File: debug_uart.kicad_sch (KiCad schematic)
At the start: 1 part, among them U1 NX1H35 PBGA625

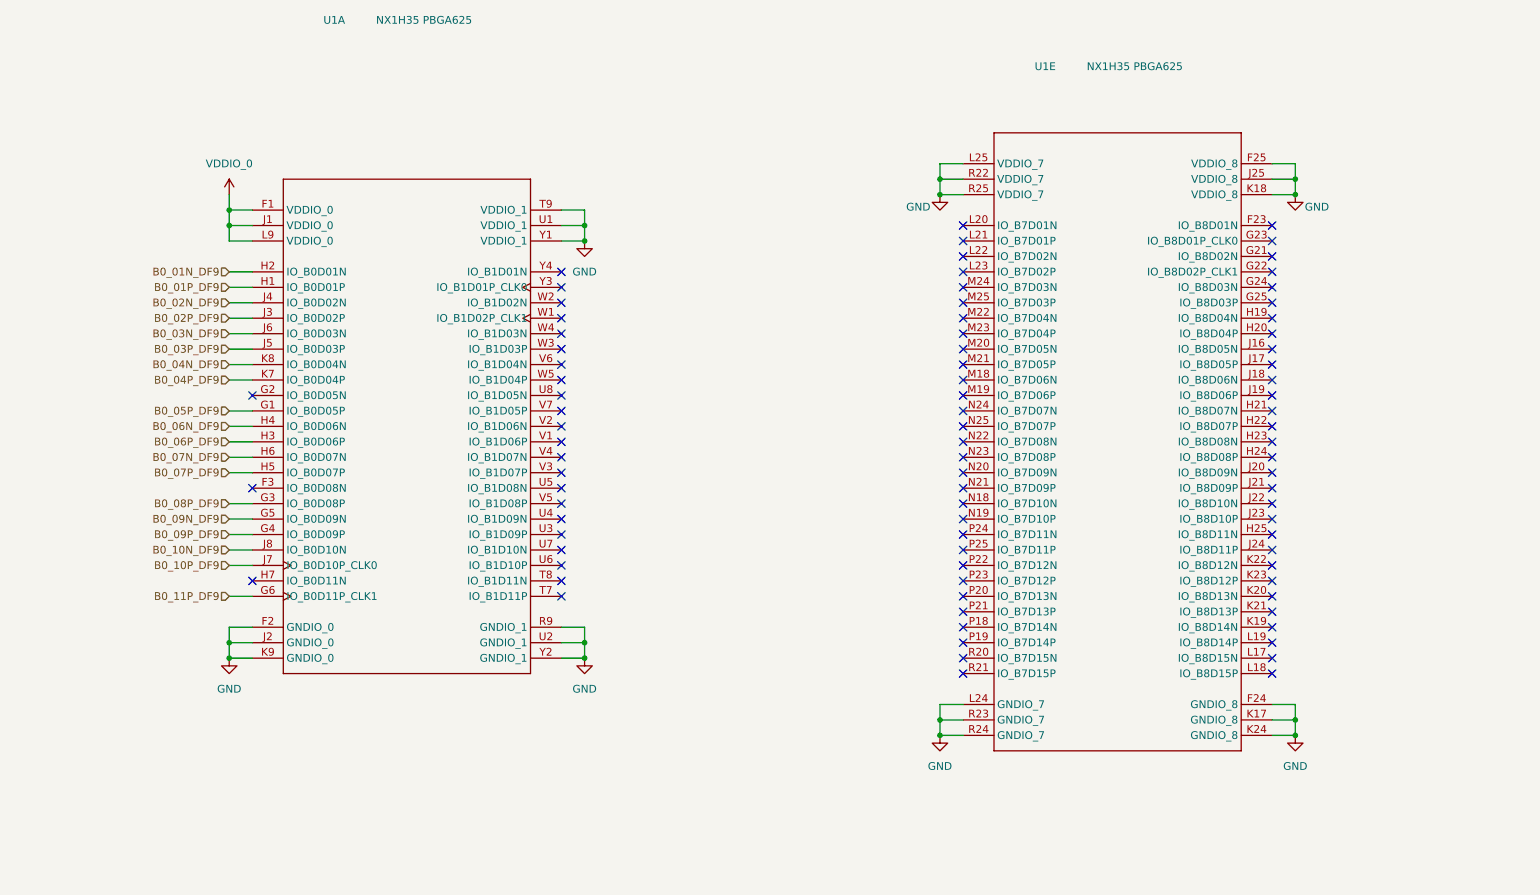
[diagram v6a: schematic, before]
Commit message: pre order adjustments. Board symmetry
adjusted little things brought up by DFM checker of JLCPCB. Board's edges fully symmetrical on y axis. 2mm shift on x axis of the DF9s maintained
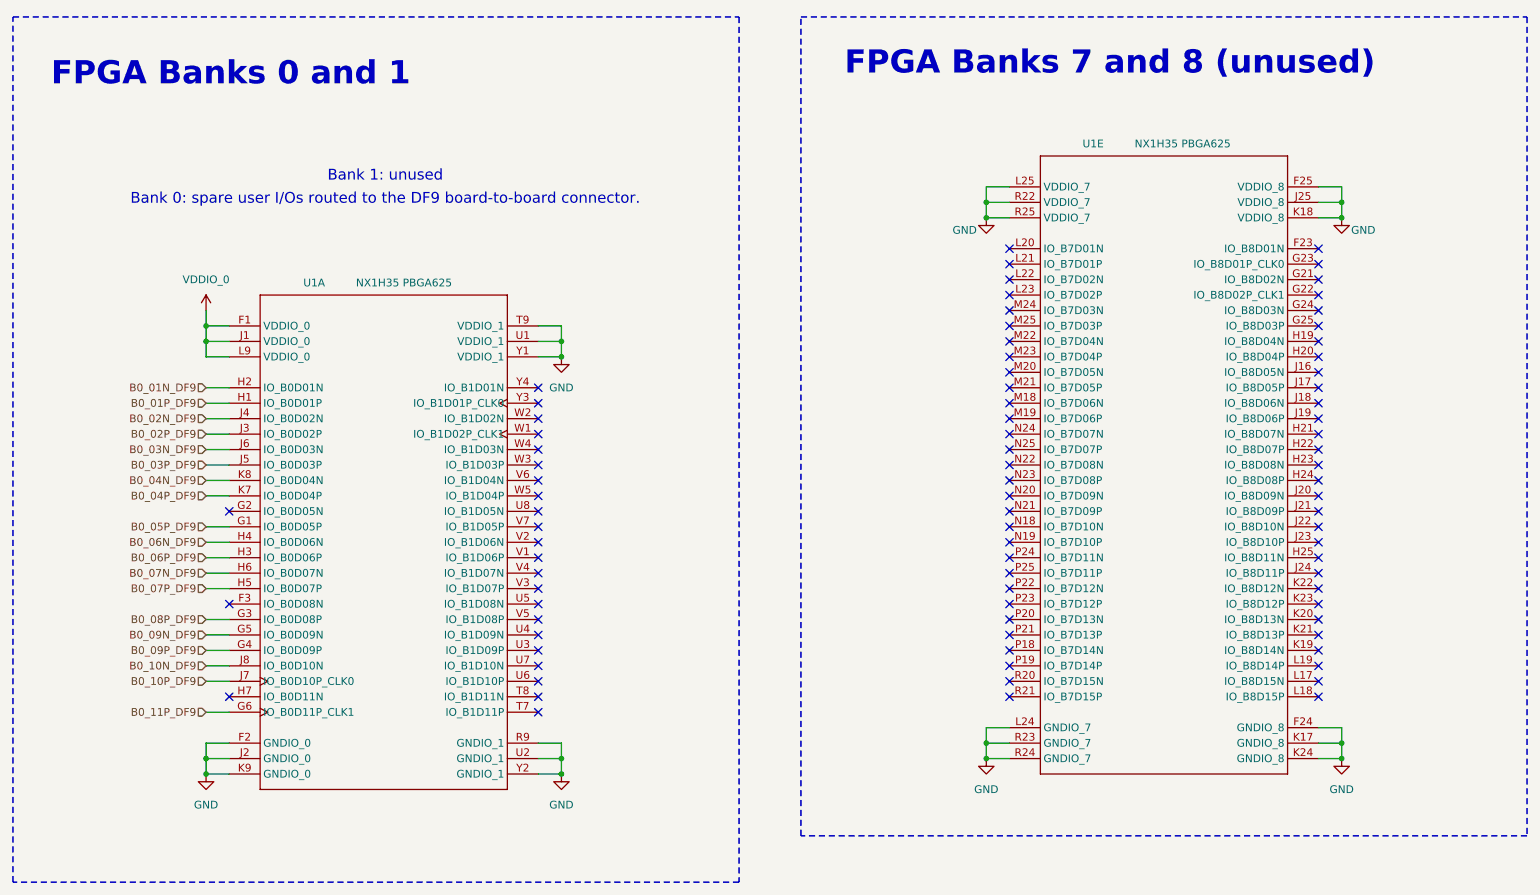
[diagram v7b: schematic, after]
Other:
- note added: "Bank 0: spare user I/Os routed to the DF9 board-to-board connector."
- note added: "Bank 1: unused"
- note added: "FPGA Banks 0 and 1"
- note added: "FPGA Banks 7 and 8 (unused)"
- moved on the sheet: U1A, U1E
